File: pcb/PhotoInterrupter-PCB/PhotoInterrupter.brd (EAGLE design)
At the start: 21 x 18.2 mm, 7 parts

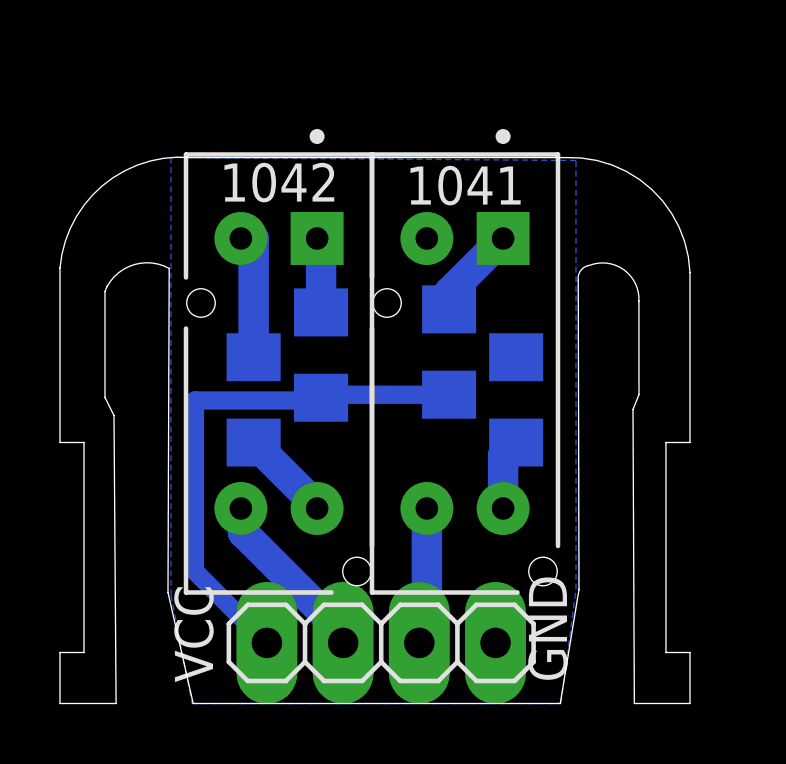
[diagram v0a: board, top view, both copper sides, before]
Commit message: Round the corners a bit more to keep from getting hit by the cam arm
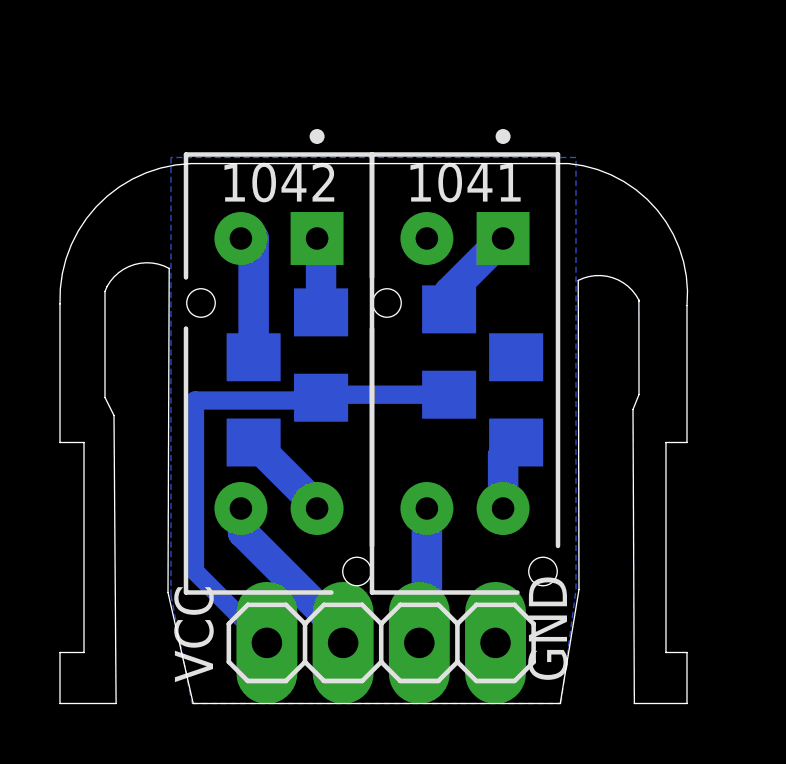
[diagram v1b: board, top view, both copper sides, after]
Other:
- board size 21 x 18.2 mm -> 20.9 x 18 mm
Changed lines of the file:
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@@
 <wire x1="16.775" y1="0.1" x2="17.4" y2="3.9" width="0" layer="20"/>
 <wire x1="17.4" y1="3.9" x2="17.375" y2="14.2025" width="0" layer="20"/>
-<wire x1="17.375" y1="14.2025" x2="17.745" y2="14.7025" width="0" layer="20" curve="-90"/>
-<wire x1="17.745" y1="14.7025" x2="19.39769375" y2="13.51279375" width="0" layer="20" curve="-114.272013"/>
+<wire x1="17.375" y1="14.2025" x2="19.3975" y2="13.545" width="0" layer="20" curve="-90"/>
+<wire x1="19.3975" y1="13.545" x2="19.39769375" y2="13.51279375" width="0" layer="20" curve="-114.272013" cap="flat"/>
 <wire x1="19.39769375" y1="13.51279375" x2="19.4" y2="10.4" width="0" layer="20"/>
 <wire x1="19.4" y1="10.4" x2="19.2" y2="9.9" width="0" layer="20"/>
 <wire x1="19.2" y1="9.9" x2="19.245" y2="0.1" width="0" layer="20"/>
-<wire x1="19.245" y1="0.1" x2="21.1" y2="0.1" width="0" layer="20"/>
-<wire x1="21.1" y1="0.1" x2="21.1" y2="1.8" width="0" layer="20"/>
-<wire x1="21.1" y1="1.8" x2="20.3" y2="1.8" width="0" layer="20"/>
+<wire x1="19.245" y1="0.1" x2="21" y2="0.1" width="0" layer="20"/>
+<wire x1="21" y1="0.1" x2="21" y2="1.8" width="0" layer="20"/>
+<wire x1="21" y1="1.8" x2="20.3" y2="1.8" width="0" layer="20"/>
 <wire x1="20.3" y1="1.8" x2="20.3" y2="8.8" width="0" layer="20"/>
-<wire x1="20.3" y1="8.8" x2="21.1" y2="8.8" width="0" layer="20"/>
-<wire x1="21.1" y1="8.8" x2="21.1" y2="14.4641" width="0" layer="20"/>
-<wire x1="21.1" y1="14.4641" x2="16.955" y2="18.2975" width="0" layer="20" curve="90"/>
-<wire x1="16.955" y1="18.2975" x2="4.46" y2="18.2975" width="0" layer="20"/>
-<wire x1="4.46" y1="18.2975" x2="0.1" y2="14.62" width="0" layer="20" curve="90"/>
-<wire x1="0.1" y1="14.62" x2="0.1" y2="8.8" width="0" layer="20"/>
+<wire x1="20.3" y1="8.8" x2="21" y2="8.8" width="0" layer="20"/>
+<wire x1="21" y1="8.8" x2="21" y2="13.3641" width="0" layer="20"/>
+<wire x1="21" y1="13.3641" x2="17.055" y2="18.0975" width="0" layer="20" curve="90"/>
+<wire x1="17.055" y1="18.0975" x2="4.46" y2="18.0975" width="0" layer="20"/>
+<wire x1="4.46" y1="18.0975" x2="0.1" y2="13.42" width="0" layer="20" curve="90"/>
+<wire x1="0.1" y1="13.42" x2="0.1" y2="8.8" width="0" layer="20"/>
 <wire x1="0.1" y1="8.8" x2="0.9" y2="8.8" width="0" layer="20"/>
 <wire x1="0.9" y1="8.8" x2="0.9" y2="1.8" width="0" layer="20"/>
@@
 <wire x1="3.7" y1="3.8" x2="4.54" y2="0.1" width="0" layer="20"/>
 <text x="5.5" y="18.1" size="1.27" layer="26" rot="MR180">1042</text>
-<text x="11.8" y="18" size="1.27" layer="26" rot="MR180">1041</text>
-<text x="15.6" y="18" size="1.27" layer="25" rot="R180">1041</text>
+<text x="11.8" y="18.1" size="1.27" layer="26" rot="MR180">1041</text>
+<text x="15.6" y="18.1" size="1.27" layer="25" rot="R180">1041</text>
 <text x="9.4" y="18.1" size="1.27" layer="25" rot="R180">1042</text>
 <text x="17" y="0.8" size="1.27" layer="25" rot="R90">GND</text>
@@
 <vertex x="16.8" y="0.1"/>
 <vertex x="17.3" y="3.9"/>
-<vertex x="17.3" y="18.2"/>
+<vertex x="17.3" y="18.3"/>
 <vertex x="3.8" y="18.3"/>
 <vertex x="3.8" y="3.7"/>

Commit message: Snap In Photo Interrupter Enhancements.
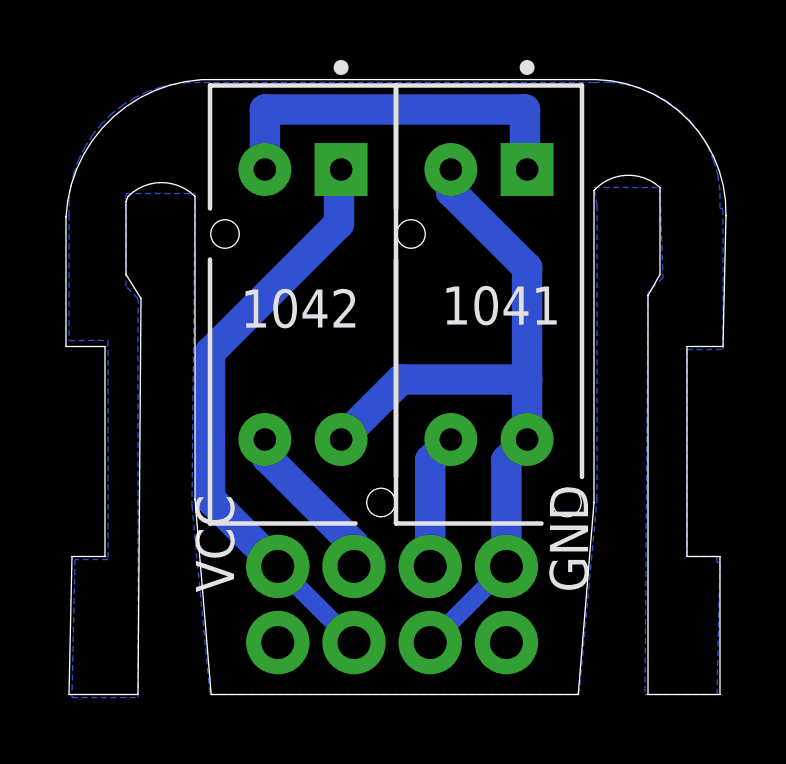
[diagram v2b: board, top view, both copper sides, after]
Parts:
- removed JP2: (no value), pinhead:1X04
- removed R1, R2: 220, resistor:R1206
- removed R3, R4: 2k2, resistor:R1206
- added K3: 61200821621, Wuerth_Elektronik_eiCan_05_Box_Header_IDC_Connectors_1_2:61200821621
- moved EE-SX1041 2.44 mm to (14.4, 13.4)
- moved EE-SX1042 2.44 mm to (8.20, 13.4)
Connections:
- removed net N$11: EE-SX1041.E, R4.1
- removed net N$2: EE-SX1041.A, R2.2
- removed net N$3: EE-SX1042.E, R3.1
- net GND: now also EE-SX1041.E, EE-SX1042.E, K3.6, K3.7; no longer EE-SX1042.K, JP2.4, R3.2, R4.2
- net HOME: now also K3.5; no longer JP2.3
- net N$1: now also EE-SX1041.A, EE-SX1042.K; no longer EE-SX1042.A, R1.2
- net POSITION: now also K3.3; no longer JP2.2
- net VCC: now also EE-SX1042.A, K3.1, K3.4; no longer JP2.1, R1.1, R2.1
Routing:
- net GND: track 4.38 -> 25.5 mm
- net N$1: track 2.60 -> 12.7 mm
- net N$2: track 3.11 -> 0.00 mm
- net N$3: track 3.07 -> 0.00 mm
- net N$11: track 2.38 -> 0.00 mm
- net VCC: track 17.7 -> 19.6 mm
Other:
- board size 20.9 x 18 mm -> 22 x 20.5 mm

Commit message: Label parts properly HY870-L and EE-SX1042 components
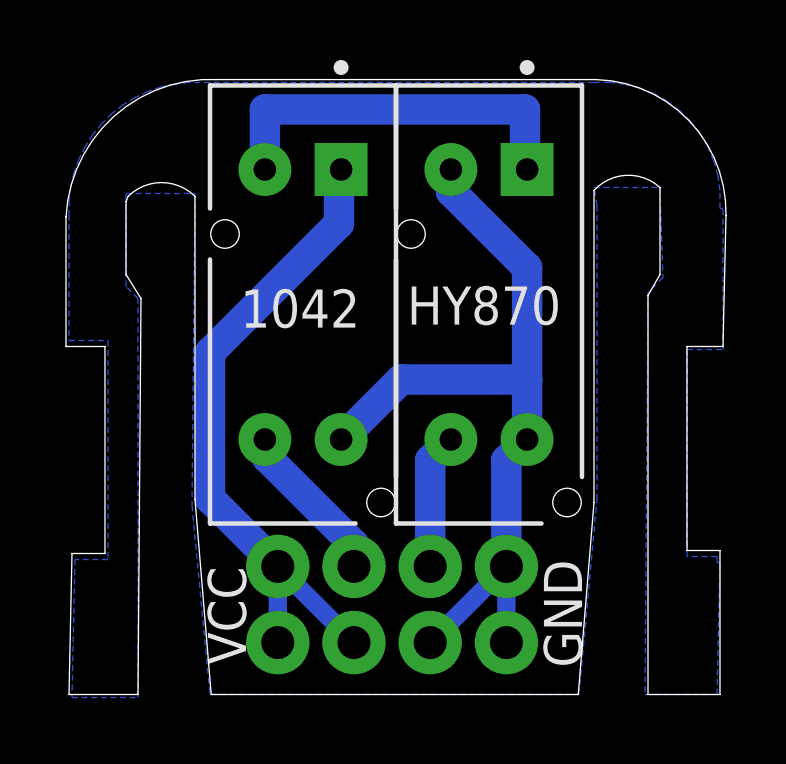
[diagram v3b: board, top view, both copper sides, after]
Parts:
- renumbered EE-SX1041 to HY870-L
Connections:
- net GND: now also K3.8
- net VCC: now also K3.2
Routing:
- net VCC: track 19.6 -> 22.1 mm
- net GND: track 25.5 -> 28.1 mm
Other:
- outline, holes or cut-outs redrawn
- board text added: "HY870"
- board text removed: "1041"
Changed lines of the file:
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@@
 <wire x1="19.7" y1="13.7" x2="19.7" y2="0.4" width="0" layer="20"/>
 <wire x1="19.7" y1="0.4" x2="22.1" y2="0.4" width="0" layer="20"/>
-<wire x1="22.1" y1="0.4" x2="22.1" y2="5" width="0" layer="20"/>
-<wire x1="22.1" y1="5" x2="21" y2="5" width="0" layer="20"/>
-<wire x1="21" y1="5" x2="21" y2="12" width="0" layer="20"/>
+<wire x1="22.1" y1="0.4" x2="22.1" y2="5.2" width="0" layer="20"/>
+<wire x1="22.1" y1="5.2" x2="21" y2="5.2" width="0" layer="20"/>
+<wire x1="21" y1="5.2" x2="21" y2="12" width="0" layer="20"/>
 <wire x1="21" y1="12" x2="22.2" y2="12" width="0" layer="20"/>
 <wire x1="22.2" y1="12" x2="22.3" y2="16.3641" width="0" layer="20"/>
@@
 <wire x1="0.3" y1="16.32" x2="0.3" y2="12" width="0" layer="20"/>
 <wire x1="0.3" y1="12" x2="1.6" y2="12" width="0" layer="20"/>
-<wire x1="1.6" y1="12" x2="1.6" y2="5" width="0" layer="20"/>
-<wire x1="1.6" y1="5" x2="0.5" y2="5" width="0" layer="20"/>
-<wire x1="0.5" y1="5" x2="0.4" y2="0.4" width="0" layer="20"/>
+<wire x1="1.6" y1="12" x2="1.6" y2="5.1" width="0" layer="20"/>
+<wire x1="1.6" y1="5.1" x2="0.5" y2="5.1" width="0" layer="20"/>
+<wire x1="0.5" y1="5.1" x2="0.4" y2="0.4" width="0" layer="20"/>
 <wire x1="0.4" y1="0.4" x2="2.7" y2="0.4" width="0" layer="20"/>
 <wire x1="2.7" y1="0.4" x2="2.8" y2="13.6" width="0" layer="20"/>
@@
 <wire x1="4.6" y1="6.9" x2="5.14" y2="0.4" width="0" layer="20"/>
 <text x="6" y="7.5" size="1.27" layer="26" rot="MR180">1042</text>
-<text x="12.2" y="7.5" size="1.27" layer="26" rot="MR180">1041</text>
-<text x="16.8" y="14" size="1.27" layer="25" rot="R180">1041</text>
+<text x="12.2" y="7.5" size="1.27" layer="26" rot="MR180">HY870</text>
+<text x="16.8" y="14" size="1.27" layer="25" rot="R180">HY870</text>
 <text x="10.1" y="13.9" size="1.27" layer="25" rot="R180">1042</text>
-<text x="17.7" y="3.8" size="1.27" layer="25" rot="R90">GND</text>
-<text x="5.9" y="3.8" size="1.27" layer="25" rot="R90">VCC</text>
+<text x="17.5" y="1.3" size="1.27" layer="25" rot="R90">GND</text>
+<text x="6.3" y="1.4" size="1.27" layer="25" rot="R90">VCC</text>
 </plain>
 <attributes>
@@
 <attribute name="PACKAGE" value="PTH_14MM4_6MM0" x="8.2" y="13.4" size="1.778" layer="27" rot="R270" display="off"/>
 </element>
-<element name="EE-SX1041" library="PhotoInterrupter" package="OMRON_ELECTRONICS_INC-EMC_DIV_EE-SX1041_0" value="OMRON_ELECTRONICS_INC-EMC_DIV_EE-SX1041OMRON_ELECTRONICS_INC-EMC_DIV_EE-SX1041_0_0" x="14.4" y="13.4" smashed="yes" rot="R270">
+<element name="HY870-L" library="PhotoInterrupter" package="OMRON_ELECTRONICS_INC-EMC_DIV_EE-SX1041_0" value="OMRON_ELECTRONICS_INC-EMC_DIV_EE-SX1041OMRON_ELECTRONICS_INC-EMC_DIV_EE-SX1041_0_0" x="14.4" y="13.4" smashed="yes" rot="R270">
 <attribute name="MPN" value="EE-SX1041" x="14.4" y="13.4" size="1.778" layer="27" rot="R270" display="off"/>
 <attribute name="MFG_PACKAGE_IDENT" value="EE-SX1041" x="14.4" y="13.4" size="1.778" layer="27" rot="R270" display="off"/>
@@
 <wire x1="5.1" y1="6.93" x2="7.36" y2="4.67" width="1.016" layer="16"/>
 <wire x1="7.36" y1="4.67" x2="9.9" y2="2.13" width="0.6096" layer="16"/>
+<contactref element="K3" pad="2"/>
+<wire x1="7.36" y1="4.67" x2="7.36" y2="2.13" width="0.6096" layer="16"/>
 </signal>
 <signal name="GND">
@@
 <vertex x="4.5" y="6.7"/>
 </polygon>
-<contactref element="EE-SX1041" pad="K"/>
+<contactref element="HY870-L" pad="K"/>
 <contactref element="EE-SX1042" pad="E"/>
-<contactref element="EE-SX1041" pad="E"/>
+<contactref element="HY870-L" pad="E"/>
 <wire x1="13.13" y1="17.9" x2="13.13" y2="17.17" width="1.016" layer="16"/>
 <wire x1="13.13" y1="17.17" x2="15.67" y2="14.63" width="1.016" layer="16"/>
@@
 <wire x1="14.98" y1="8.21" x2="15.67" y2="8.9" width="1.016" layer="16"/>
 <wire x1="14.98" y1="4.67" x2="12.44" y2="2.13" width="0.6096" layer="16"/>
+<contactref element="K3" pad="8"/>
+<wire x1="14.98" y1="4.67" x2="14.98" y2="2.13" width="0.6096" layer="16"/>
 </signal>
 <signal name="HOME">
-<contactref element="EE-SX1041" pad="C"/>
+<contactref element="HY870-L" pad="C"/>
 <wire x1="12.8775" y1="8.6475" x2="13.13" y2="8.9" width="1.016" layer="16"/>
 <contactref element="K3" pad="5"/>
@@
 <signal name="N$1">
 <contactref element="EE-SX1042" pad="K"/>
-<contactref element="EE-SX1041" pad="A"/>
+<contactref element="HY870-L" pad="A"/>
 <wire x1="6.93" y1="17.9" x2="6.93" y2="19.9" width="1.016" layer="16"/>
 <wire x1="6.93" y1="19.9" x2="15.6" y2="19.9" width="1.016" layer="16"/>
